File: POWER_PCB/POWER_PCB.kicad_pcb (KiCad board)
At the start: 2 copper layers, 70 x 50 mm, 66 parts, among them J1 10103594-0001LF, J10 Conn_01x02, J2 Barrel_Jack, J3 Conn_01x02, J4 Conn_01x02, J5 Conn_01x02, J6 Conn_01x02, J7 Conn_01x01, J8 Conn_01x01, J9 Conn_01x01, Q1 Q_PMOS_GDS, Q2 Q_NMOS_GSD, Q3 Q_NMOS_GSD, Q4 Q_PMOS_GDS, U1 TS462CDT, U2 TPS55340PWP

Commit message: Finished controller layout, and 80% done with power PCB layout.
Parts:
- moved C14 0.74 mm to (93.4, 65.8)
- moved R10 0.74 mm to (103.9, 71.9)
- moved R11 0.74 mm to (100.0, 72.8)
- moved R12 0.74 mm to (103.8, 69.0)
- moved R13 0.74 mm to (100.0, 68.4)
- moved U1 0.74 mm to (94.4, 70.7)
- moved TP10 0.64 mm to (104.6, 74.6)
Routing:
- net GND: track 0.00 -> 59.0 mm, vias 0 -> 21
- net Vin: track 0.00 -> 55.7 mm, vias 0 -> 1
- net BOOST_EN: track 0.00 -> 52.5 mm, vias 0 -> 3
- net /Input_Output/Vout: track 0.00 -> 45.6 mm
- net Net-(J10-Pad2): track 0.00 -> 40.8 mm
- net LED_RTN: track 0.00 -> 23.7 mm
- net Net-(C1-Pad2): track 5.45 -> 19.8 mm
- net Net-(J10-Pad1): track 0.00 -> 14.2 mm
- net Net-(Q4-Pad1): track 0.00 -> 12.4 mm
- net BOOST_BYPASS: track 0.00 -> 12.1 mm, vias 0 -> 1
- net Net-(C10-Pad1): track 0.00 -> 7.00 mm
- net Net-(R12-Pad1): track 0.00 -> 6.29 mm
- net Net-(U1-Pad6): track 0.00 -> 6.28 mm
- net Net-(R10-Pad1): track 0.00 -> 6.24 mm
- net Net-(R14-Pad1): track 0.00 -> 5.60 mm
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- added copper zone on F.Cu, net BOOST_OUT
- added copper zone on F.Cu, net GND
- added copper zone on In1.Cu, net GND
- added copper zone on In2.Cu, net GND
- added copper zone on F.Cu, net Net-(C1-Pad2)
- added copper zone on B.Cu, net Net-(C2-Pad1)
- added copper zone on F.Cu, net Net-(C2-Pad1)
- added copper zone on B.Cu, net Net-(C3-Pad1)
- added copper zone on B.Cu, net Net-(C4-Pad1)
- added copper zone on F.Cu, net Net-(C6-Pad1)
- added copper zone on F.Cu, net Net-(C8-Pad1)
- added copper zone on F.Cu, net Net-(D2-Pad1)
- added copper zone on F.Cu, net Vin
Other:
- copper layers 2 -> 4

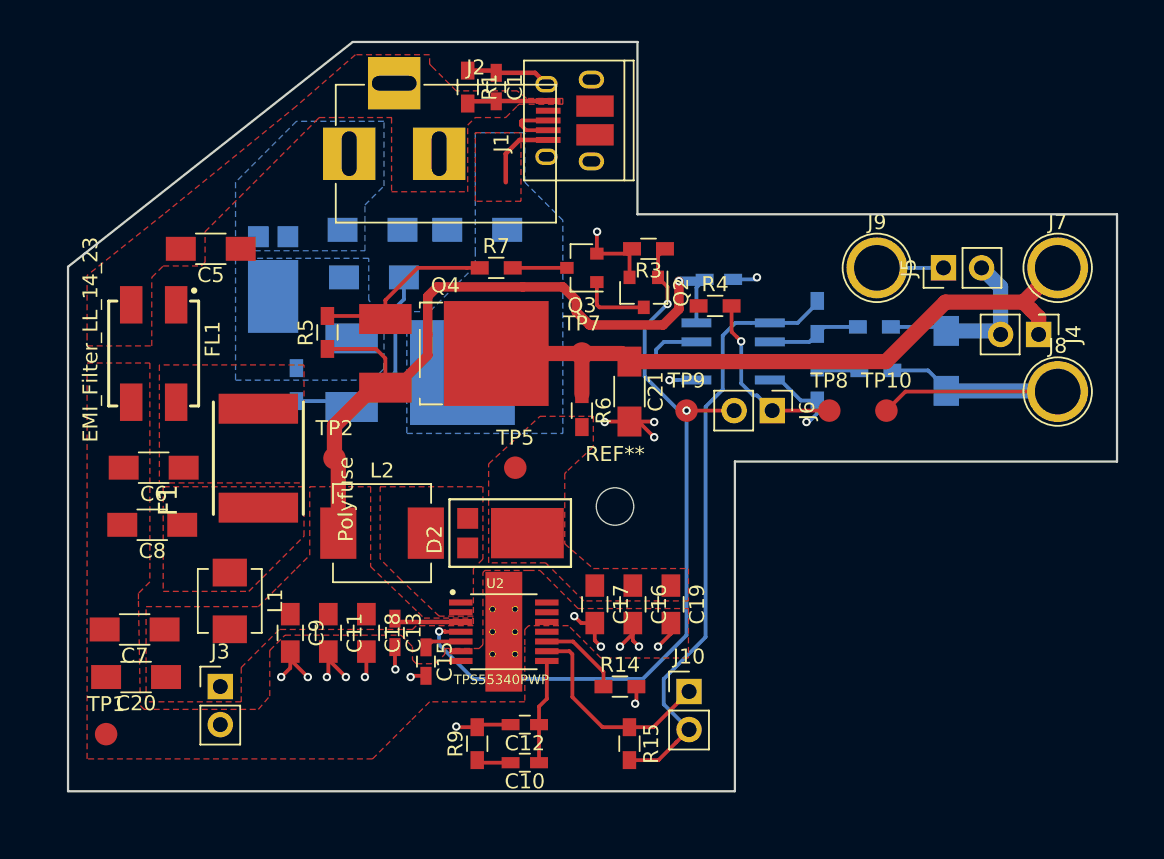
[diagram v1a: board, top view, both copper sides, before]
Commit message: Finished copper, silkscreen and gerbers for power PCB and controller PCBs,
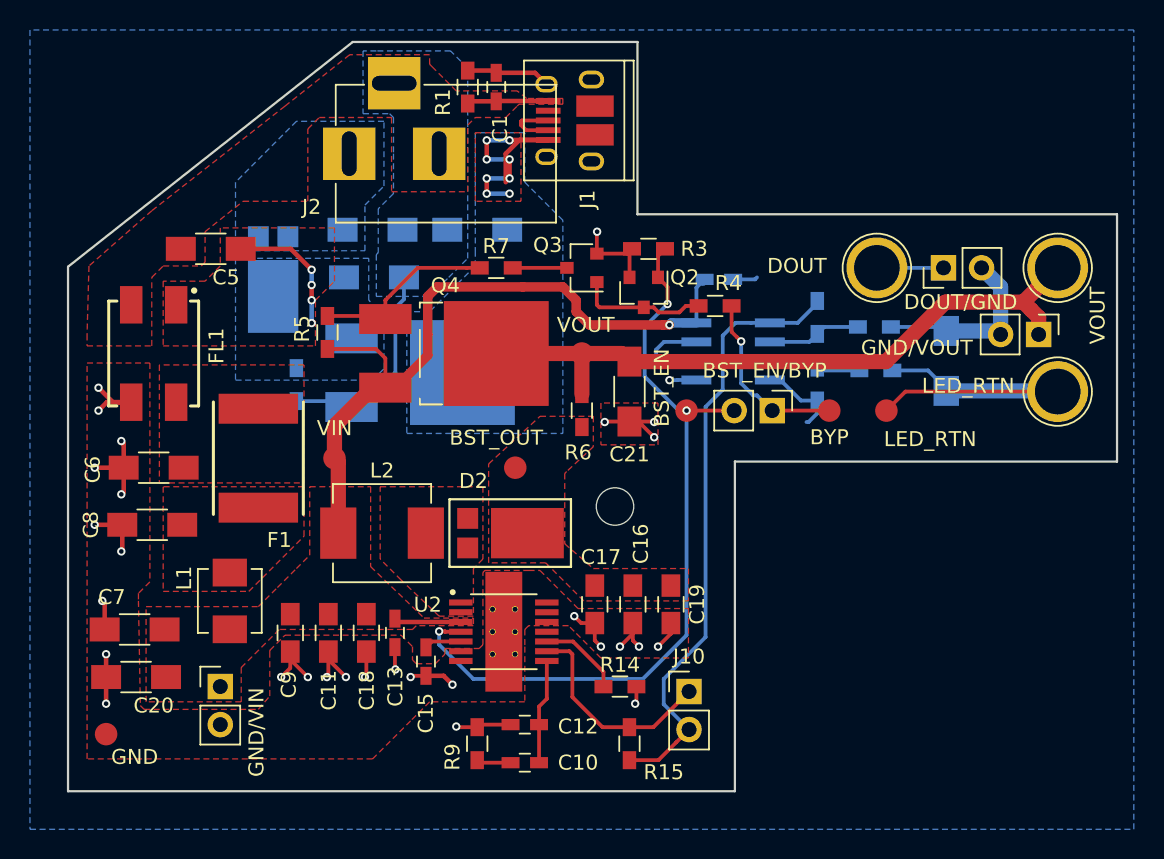
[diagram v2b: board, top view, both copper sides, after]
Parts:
- renumbered TP9 to BST_EN, J6 to BST_EN/BYP, TP5 to BST_OUT, TP8 to BYP, J9 to DOUT, J5 to DOUT/GND, TP1 to GND, J3 to GND/VIN, J4 to GND/VOUT, J8 to LED_RTN, TP10 to LED_RTN, TP2 to VIN, J7 to VOUT, TP7 to VOUT
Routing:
- net GND: track 59.0 -> 80.5 mm, vias 21 -> 30
- net Net-(C2-Pad1): track 5.12 -> 17.4 mm, vias 0 -> 8
- net Net-(C4-Pad1): track 0.00 -> 8.87 mm, vias 0 -> 4
- net Net-(Q2-Pad3): track 4.72 -> 8.70 mm
- net Vin: track 55.7 -> 53.0 mm
- added copper zone on B.Cu, net GND
- added copper zone on B.Cu, net Net-(C1-Pad2)
- added copper zone on F.Cu, net Net-(C4-Pad1)
- removed copper zone on In1.Cu, net GND
- removed copper zone on In2.Cu, net GND
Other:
- copper layers 4 -> 2
- board text added: "POWER_PCB Rev01"
